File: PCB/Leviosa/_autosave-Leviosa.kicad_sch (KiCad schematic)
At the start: 24 parts, among them Q3 TIP122, Q4 TIP122, U1 LM324, U5 L7805, U6 SS495A

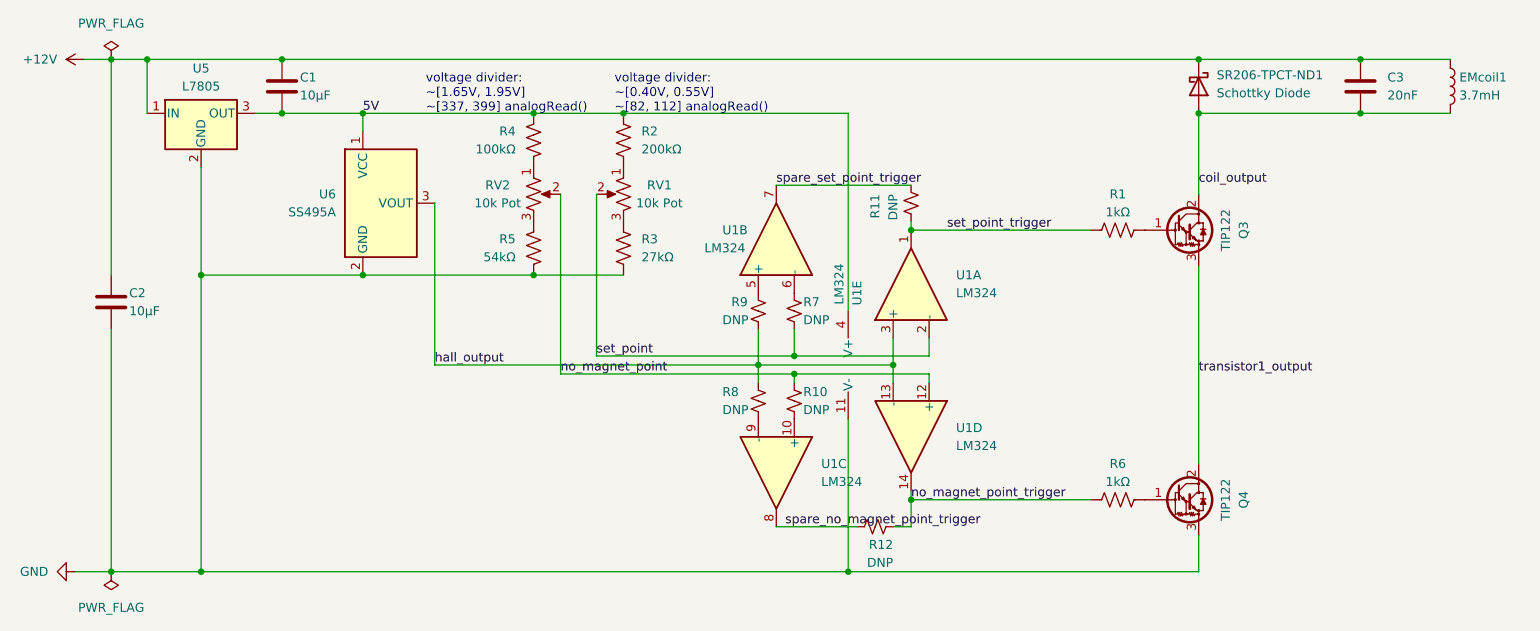
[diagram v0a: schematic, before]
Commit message: update PCB with some of Jack's feedback
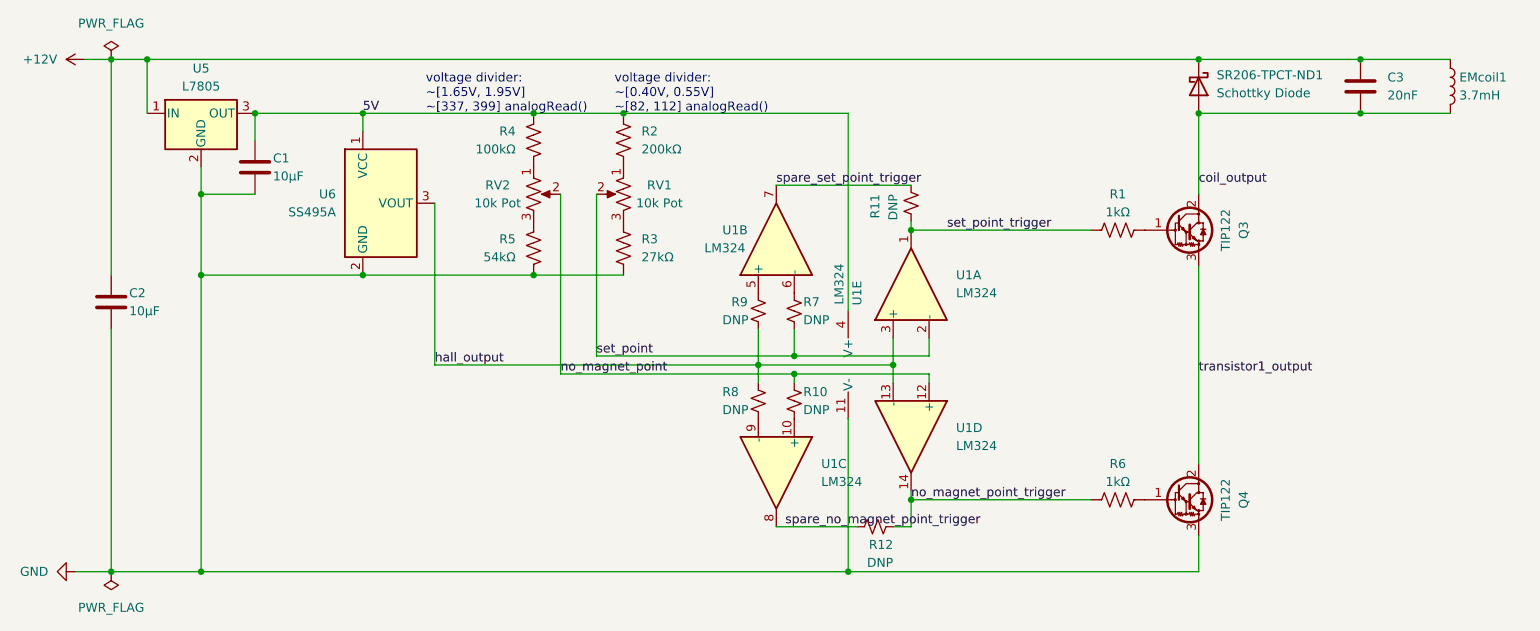
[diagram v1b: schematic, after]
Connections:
- net +12V: no longer C1.1
- net 5V: now also C1.1; no longer C1.2
- net GND: now also C1.2
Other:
- moved on the sheet: C1
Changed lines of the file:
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@@
   (junction (at 187.96 116.84) (diameter 0) (color 0 0 0 0)
   )
+  (junction (at 95.25 62.23) (diameter 0) (color 0 0 0 0)
+  )
   (junction (at 110.49 62.23) (diameter 0) (color 0 0 0 0)
   )
   (junction (at 228.6 62.23) (diameter 0) (color 0 0 0 0)
   )
-  (junction (at 99.06 62.23) (diameter 0) (color 0 0 0 0)
-  )
   (junction (at 87.63 127) (diameter 0) (color 0 0 0 0)
   )
@@
   (junction (at 171.45 99.06) (diameter 0) (color 0 0 0 0)
   )
-  (junction (at 99.06 54.61) (diameter 0) (color 0 0 0 0)
-  )
   (junction (at 110.49 85.09) (diameter 0) (color 0 0 0 0)
   )
+  (junction (at 87.63 73.66) (diameter 0) (color 0 0 0 0)
+  )
   (junction (at 74.93 127) (diameter 0) (color 0 0 0 0)
   )
@@
     (stroke (width 0) (type default))
   )
+  (wire (pts (xy 87.63 73.66) (xy 95.25 73.66))
+    (stroke (width 0) (type default))
+  )
   (wire (pts (xy 166.37 100.33) (xy 166.37 97.79))
     (stroke (width 0) (type default))
@@
     (stroke (width 0) (type default))
   )
-  (wire (pts (xy 80.01 54.61) (xy 99.06 54.61))
+  (wire (pts (xy 80.01 54.61) (xy 228.6 54.61))
     (stroke (width 0) (type default))
   )
@@
     (stroke (width 0) (type default))
   )
-  (wire (pts (xy 95.25 62.23) (xy 99.06 62.23))
+  (wire (pts (xy 95.25 62.23) (xy 110.49 62.23))
     (stroke (width 0) (type default))
   )
@@
     (stroke (width 0) (type default))
   )
+  (wire (pts (xy 87.63 73.66) (xy 87.63 85.09))
+    (stroke (width 0) (type default))
+  )
   (wire (pts (xy 87.63 85.09) (xy 110.49 85.09))
     (stroke (width 0) (type default))
@@
     (stroke (width 0) (type default))
   )
-  (wire (pts (xy 110.49 62.23) (xy 99.06 62.23))
+  (wire (pts (xy 95.25 62.23) (xy 95.25 66.04))
     (stroke (width 0) (type default))
   )
@@
     (stroke (width 0) (type default))
   )
-  (wire (pts (xy 99.06 54.61) (xy 228.6 54.61))
-    (stroke (width 0) (type default))
-  )
   (wire (pts (xy 74.93 92.71) (xy 74.93 127))
     (stroke (width 0) (type default))
@@
     (stroke (width 0) (type default))
   )
-  (wire (pts (xy 87.63 69.85) (xy 87.63 85.09))
+  (wire (pts (xy 87.63 69.85) (xy 87.63 73.66))
     (stroke (width 0) (type default))
   )
@@
     )
   )
-  (symbol (lib_id "Device:C") (at 99.06 58.42 0) (unit 1)
+  (symbol (lib_id "Device:C") (at 95.25 69.85 0) (unit 1)
     (in_bom yes) (on_board yes) (dnp no)
-    (property "Reference" "C1" (at 101.6 57.15 0)
+    (property "Reference" "C1" (at 97.79 68.58 0)
       (effects (font (size 1.27 1.27)) (justify left))
     )
-    (property "Value" "10µF" (at 101.6 59.69 0)
+    (property "Value" "10µF" (at 97.79 71.12 0)
       (effects (font (size 1.27 1.27)) (justify left))
     )
-    (property "Footprint" "Capacitor_THT:CP_Axial_L10.0mm_D6.0mm_P15.00mm_Horizontal" (at 100.0252 62.23 0)
-      (effects (font (size 1.27 1.27)) hide)
-    )
-    (property "Datasheet" "~" (at 99.06 58.42 0)
-      (effects (font (size 1.27 1.27)) hide)
-    )
+    (property "Footprint" "Capacitor_THT:CP_Axial_L10.0mm_D6.0mm_P15.00mm_Horizontal" (at 96.2152 73.66 0)
+      (effects (font (size 1.27 1.27)) hide)
+    )
+    (property "Datasheet" "~" (at 95.25 69.85 0)
+      (effects (font (size 1.27 1.27)) hide)
+    )
